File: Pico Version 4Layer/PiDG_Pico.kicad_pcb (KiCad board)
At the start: 4 copper layers, 126 x 126 mm, 71 parts, among them J1 Conn_02x05_Odd_Even, J10 Trig, J11 Laser Enable, J12 Pixel Reset, J14 Pico Socket A, J15 Pico Socket B, J16 Laser En/PWM Trig/GND, J17 USB-C PD in, J2 Conn_02x05_Odd_Even, J3 Conn_02x05_Odd_Even, J4 Conn_02x05_Odd_Even, J5 Conn_02x05_Odd_Even, J6 Conn_02x05_Odd_Even, J7 Laser 1, J8 Laser 2, U1 74LVC1G04, U10 74AHCT1G08, U12 74LVC1G17, U13 UCC27524, U14 CH224K, U15 AP63205WU, U16 LM66100, U17 LP2951D, U2 SN74LVC04AD, U3 74LVC1G04, U4 SN74LVC04AD, U5 74LVC1G04, U6 SN74LVC04AD, U7 74AHCT1G08, U8 74AHCT1G08, U9 NCP718xSN180

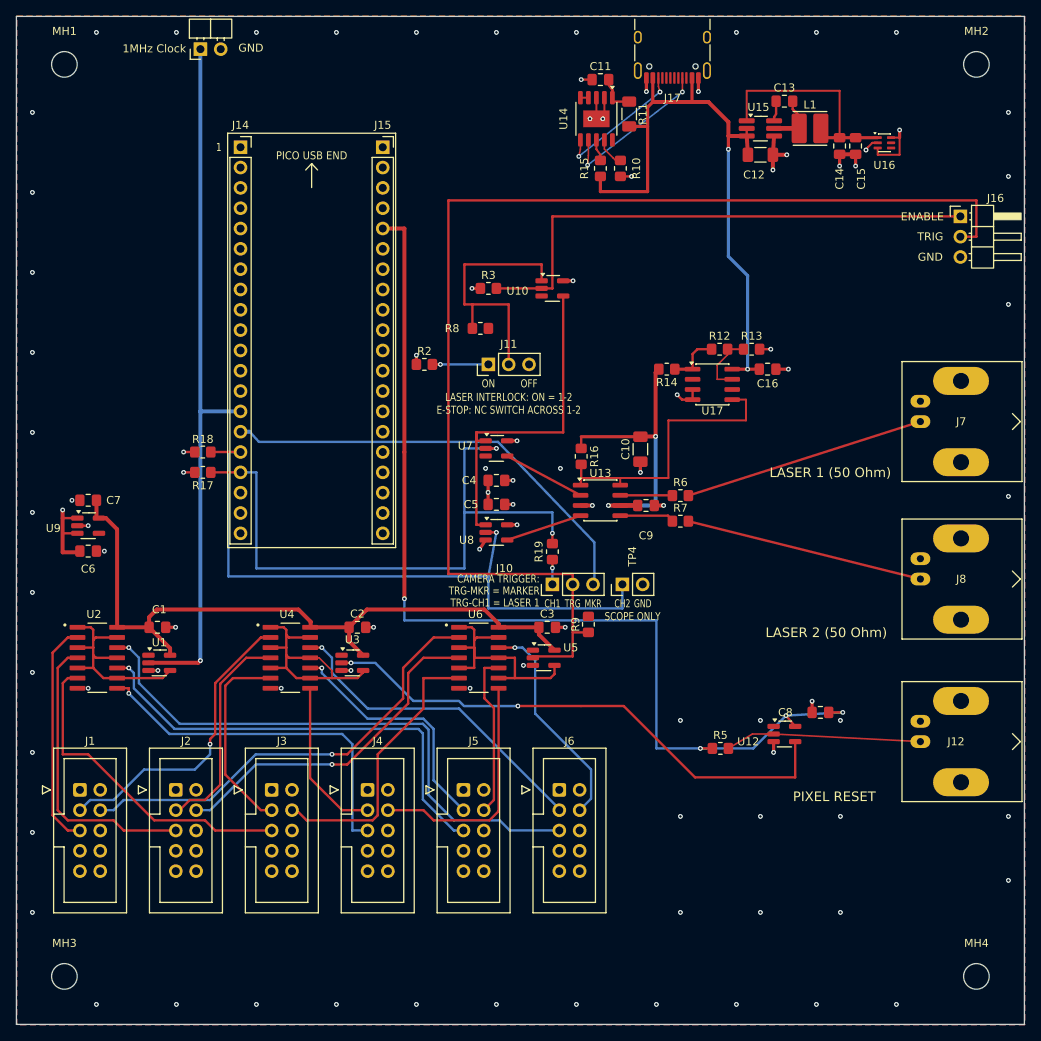
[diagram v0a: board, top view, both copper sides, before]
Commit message: Move the Pico to the top edge; label the control and power USB ports
J14/J15 and R17/R18 shifted 13.97 mm up so the Pico's micro-USB reaches the
top board edge for an enclosure cut-out. GP10-13 and 3V3 traces stretched;
PWM_Trig re-entered right of the CH1 run (crosses J15 between two unused
pads as before). CH1/CH2 lengthen equally. TP3 moved 3 mm left for socket
clearance with its spur re-jogged. Silkscreen: CONTROL / PROGRAM - PICO
MICRO-USB and POWER ONLY - USB-C PD 15 V at the two ports. DRC 0/0, all 334
pads match the schematic; gerbers, drills, zip and both placement files
regenerated; README, Hardware.md and JLC checklist updated.

Co-Authored-By: Claude Opus 5.5 (1M context) <noreply@anthropic.com>
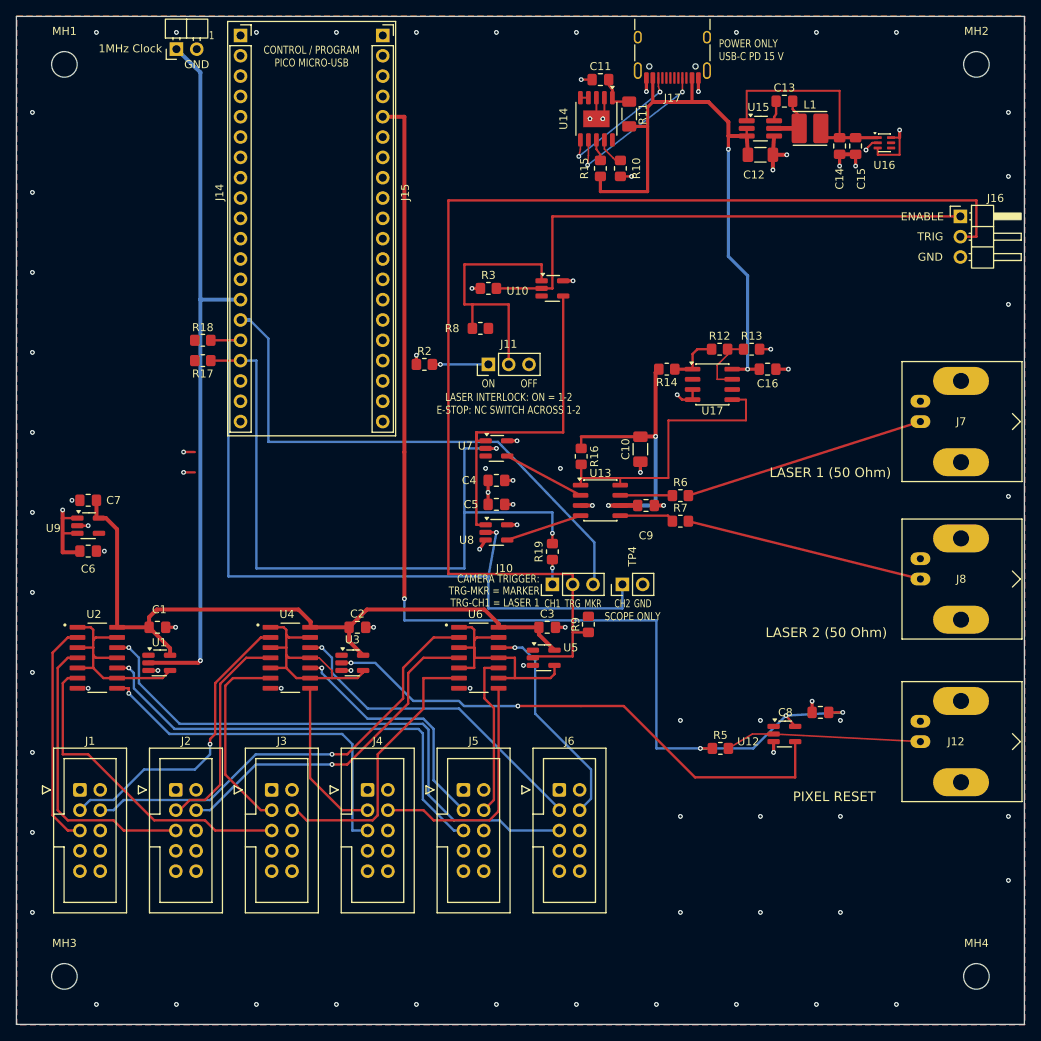
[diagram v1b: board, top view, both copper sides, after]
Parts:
- moved J14 14.0 mm to (160.0, 32.4)
- moved J15 14.0 mm to (177.8, 32.4)
- moved R17 14.0 mm to (155.3, 73.0)
- moved R18 14.0 mm to (155.3, 70.5)
- moved TP3 3.00 mm to (152.0, 34.1)
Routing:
- net _PULSE_OUT_CH2: track 84.0 -> 97.9 mm
- net _PULSE_OUT_CH1: track 79.0 -> 92.9 mm
- net +3V3: track 129.2 -> 143.2 mm
- net PWM_Trig: track 55.5 -> 68.8 mm
- net PWM_1MHz: track 88.1 -> 89.3 mm
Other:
- board text added: "CONTROL / PROGRAM"
- board text added: "PICO MICRO-USB"
- board text added: "POWER ONLY"
- board text added: "USB-C PD 15 V"
- board text removed: "PICO USB END"
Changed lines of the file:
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@@
 	(footprint "Connector_PinSocket_2.54mm:PinSocket_1x20_P2.54mm_Vertical"
 		(layer "F.Cu")
-		(at 177.795 46.355)
+		(at 177.795 32.385)
 		(descr "Through hole straight socket strip, 1x20, 2.54mm pitch, single row (from Kicad 4.0.7), script generated")
 		(tags "Through hole socket strip THT 1x20 2.54mm single row")
 		(property "Reference" "J15"
-			(at 0 -2.77 0)
+			(at 2.805 19.615 90)
 			(layer "F.SilkS")
 			(effects
@@
 	(footprint "Resistor_SMD:R_0805_2012Metric_Pad1.20x1.40mm_HandSolder"
 		(layer "F.Cu")
-		(at 155.3 86.995 180)
+		(at 155.3 73.025 180)
 		(descr "Resistor SMD 0805 (2012 Metric), square (rectangular) end terminal, IPC-7351 nominal with elongated pad for handsoldering. (Body size source: IPC-SM-782 page 72, https://www.pcb-3d.com/wordpress/wp-content/uploads/ipc-sm-782a_amendment_1_and_2.pdf)")
 		(tags "resistor handsolder")
@@
 	(footprint "Connector_PinSocket_2.54mm:PinSocket_1x20_P2.54mm_Vertical"
 		(layer "F.Cu")
-		(at 160.015 46.355)
+		(at 160.015 32.385)
 		(descr "Through hole straight socket strip, 1x20, 2.54mm pitch, single row (from Kicad 4.0.7), script generated")
 		(tags "Through hole socket strip THT 1x20 2.54mm single row")
 		(property "Reference" "J14"
-			(at 0 -2.77 0)
+			(at -2.615 19.615 90)
 			(layer "F.SilkS")
 			(effects
@@
 	(footprint "PiDG_Local:PinHeader_1x02_P2.54mm_Horizontal_EdgeTrim"
 		(layer "F.Cu")
-		(at 155.002076 34.093171 90)
+		(at 152.002076 34.093171 90)
 		(descr "Through hole angled pin header, 1x02, 2.54mm pitch, 6mm pin length, single row")
 		(tags "Through hole angled pin header THT 1x02 2.54mm single row")
@@
 	(footprint "Resistor_SMD:R_0805_2012Metric_Pad1.20x1.40mm_HandSolder"
 		(layer "F.Cu")
-		(at 155.3 84.455 180)
+		(at 155.3 70.485 180)
 		(descr "Resistor SMD 0805 (2012 Metric), square (rectangular) end terminal, IPC-7351 nominal with elongated pad for handsoldering. (Body size source: IPC-SM-782 page 72, https://www.pcb-3d.com/wordpress/wp-content/uploads/ipc-sm-782a_amendment_1_and_2.pdf)")
 		(tags "resistor handsolder")
@@
 	)
 	(gr_line
-		(start 158.405 44.6)
-		(end 179.405 44.6)
+		(start 158.405 30.63)
+		(end 179.405 30.63)
 		(stroke
 			(width 0.15)
@@
 	)
 	(gr_line
-		(start 158.405 96.4)
-		(end 158.405 44.6)
+		(start 158.405 82.43)
+		(end 158.405 30.63)
 		(stroke
 			(width 0.15)
@@
 	)
 	(gr_line
-		(start 168.905 48.4)
-		(end 168.155 49.2)
+		(start 179.405 30.63)
+		(end 179.405 82.43)
 		(stroke
 			(width 0.15)
@@
 	)
 	(gr_line
-		(start 168.905 48.4)
-		(end 168.905 51.4)
-		(stroke
-			(width 0.15)
-			(type default)
-		)
-		(layer "F.SilkS")
-	)
-	(gr_line
-		(start 168.905 48.4)
-		(end 169.655 49.2)
-		(stroke
-			(width 0.15)
-			(type default)
-		)
-		(layer "F.SilkS")
-	)
-	(gr_line
-		(start 179.405 44.6)
-		(end 179.405 96.4)
-		(stroke
-			(width 0.15)
-			(type default)
-		)
-		(layer "F.SilkS")
-	)
-	(gr_line
-		(start 179.405 96.4)
-		(end 158.405 96.4)
+		(start 179.405 82.43)
+		(end 158.405 82.43)
 		(stroke
 			(width 0.15)
@@
 		)
 	)
+	(gr_text "POWER ONLY"
+		(at 219.8 33.4 0)
+		(layer "F.SilkS")
+		(effects
+			(font
+				(size 1 0.8)
+				(thickness 0.15)
+			)
+			(justify left)
+		)
+	)
+	(gr_text "USB-C PD 15 V"
+		(at 219.8 35 0)
+		(layer "F.SilkS")
+		(effects
+			(font
+				(size 1 0.8)
+				(thickness 0.15)
+			)
+			(justify left)
+		)
+	)
 	(gr_text "1"
-		(at 157.3 46.355 0)
+		(at 156.4 32.384999 0)
+		(layer "F.SilkS")
+		(effects
+			(font
+				(size 1 0.8)
+				(thickness 0.15)
+			)
+		)
+	)
+	(gr_text "CONTROL / PROGRAM"
+		(at 168.905 34.2 0)
+		(layer "F.SilkS")
+		(effects
+			(font
+				(size 1 0.8)
+				(thickness 0.15)
+			)
+		)
+	)
+	(gr_text "PICO MICRO-USB"
+		(at 168.905 35.8 0)
 		(layer "F.SilkS")
 		(effects
@@
 		)
 	)
-	(gr_text "PICO USB END"
-		(at 168.905 47.4 0)
-		(layer "F.SilkS")
-		(effects
-			(font
-				(size 1 0.9)
-				(thickness 0.15)
-			)
-		)
-	)
-	(gr_text "GND"
-		(at 159.74 34.53 0)
+	(gr_text "1MHz Clock"
+		(at 146.24 34.03 0)
 		(layer "F.SilkS")
 		(effects
@@
 				(thickness 0.15)
 			)
-			(justify left bottom)
 		)
 	)
-	(gr_text "1MHz Clock"
-		(at 149.24 34.03 0)
+	(gr_text "ENABLE"
+		(at 245.24 55.03 0)
 		(layer "F.SilkS")
 		(effects
@@
 		)
 	)
-	(gr_text "ENABLE"
-		(at 245.24 55.03 0)
+	(gr_text "TRIG"
+		(at 246.24 57.53 0)
 		(layer "F.SilkS")
 		(effects
@@
 		)
 	)
-	(gr_text "TRIG"
-		(at 246.24 57.53 0)
+	(gr_text "GND"
+		(at 246.24 60.08 0)
 		(layer "F.SilkS")
 		(effects
@@
 	)
 	(gr_text "GND"
-		(at 246.24 60.08 0)
+		(at 154.54 36.6 0)
 		(layer "F.SilkS")
 		(effects
@@
 				(thickness 0.15)
 			)
+			(justify bottom)
 		)
 	)
@@
 	)
 	(segment
-		(start 177.795 56.515)
-		(end 180.5 56.515)
+		(start 177.795 42.545)
+		(end 180.5 42.545)
 		(width 0.5)
 		(layer "F.Cu")
@@
 	)
 	(segment
-		(start 180.5 56.515)
+		(start 180.5 42.545)
 		(end 180.5 84.455)
 		(width 0.5)
@@
 	)
 	(segment
-		(start 160.015 86.995)
-		(end 156.3 86.995)
+		(start 160.015 73.025)
+		(end 156.3 73.025)
 		(width 0.3)
 		(layer "F.Cu")
@@
 	(segment
 		(start 162 99)
-		(end 162 86.995)
+		(end 162 73.025)
 		(width 0.3)
 		(layer "B.Cu")
@@
 	)
 	(segment
-		(start 162 86.995)
-		(end 160.015 86.995)
+		(start 162 73.025)
+		(end 160.015 73.025)
 		(width 0.3)
 		(layer "B.Cu")
@@
 	)
 	(segment
-		(start 160.015 84.455)
-		(end 156.3 84.455)
+		(start 160.015 70.485)
+		(end 156.3 70.485)
 		(width 0.3)
 		(layer "F.Cu")
@@
 	(segment
 		(start 158.5 100)
-		(end 158.5 84.455)
+		(end 158.5 70.485)
 		(width 0.3)
 		(layer "B.Cu")
@@
 	)
 	(segment
-		(start 158.5 84.455)
-		(end 160.015 84.455)
+		(start 158.5 70.485)
+		(end 160.015 70.485)
 		(width 0.3)
 		(layer "B.Cu")
@@
 	)
 	(segment
-		(start 161.167 81.915)
-		(end 162.318 83.185)
+		(start 163.5 70.278)
+		(end 163.5 83.185)
+		(width 0.3)
+		(layer "B.Cu")
+		(net "PWM_Trig")
+	)
+	(segment
+		(start 161.167 67.945)
+		(end 163.5 70.278)
 		(width 0.3)
 		(layer "B.Cu")
@@
 	)
 	(segment
-		(start 160.015 81.915)
-		(end 161.167 81.915)
+		(start 160.015 67.945)
+		(end 161.167 67.945)
 		(width 0.5)
 		(layer "B.Cu")
@@
 	)
 	(segment
-		(start 162.318 83.185)
+		(start 163.5 83.185)
 		(end 192.2 83.185)
 		(width 0.3)
@@
 	)
 	(segment
-		(start 155 79.375)
-		(end 155 34.095247)
+		(start 155 65.405)
+		(end 155 37)
 		(width 0.5)
 		(layer "B.Cu")
@@
 	)
 	(segment
-		(start 160.015 79.375)
-		(end 155 79.375)
+		(start 160.015 65.405)
+		(end 155 65.405)
 		(width 0.5)
 		(layer "B.Cu")
@@
 	)
 	(segment
-		(start 155 79.375)
+		(start 155 65.405)
 		(end 155 110.53)
 		(width 0.5)
@@
 	)
 	(segment
-		(start 155 34.095247)
-		(end 155.002076 34.093171)
+		(start 155 37)
+		(end 152.002 34.093)
 		(width 0.5)
 		(layer "B.Cu")

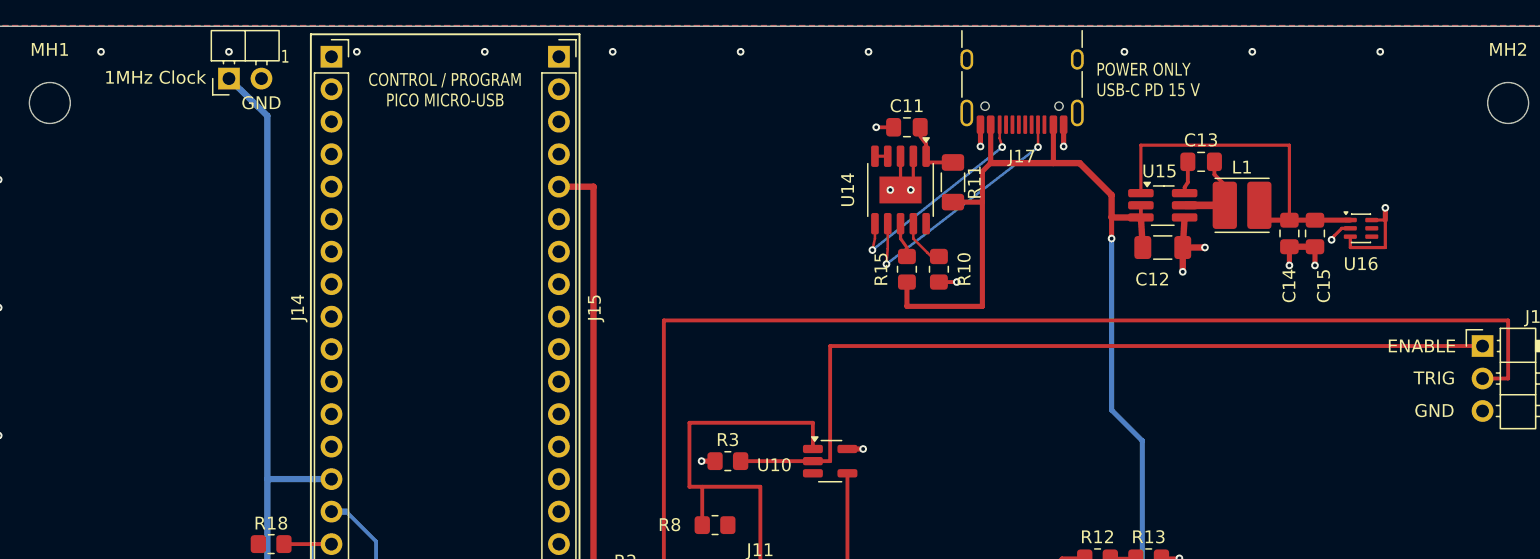
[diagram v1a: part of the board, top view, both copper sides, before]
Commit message: J16 explicit silkscreen; TP3 overhang matched to J16
J16 now reads ENABLE IN: PULL LOW = LASERS OFF / TRIG OUT: CAMERA TRIGGER
(MONITOR) / GND, plus J16: NEVER FIT A SHUNT and NOT FAIL-SAFE - PUT THE
E-STOP ON J11. TP3 moved 3.9 mm inboard so its pins overhang the top edge
by 2.1 mm, the same as J16 on the right edge (spur re-jogged, labels moved).
DRC 0/0; gerbers, drills, zip and placement files regenerated; README,
Hardware.md and JLC checklist updated.

Co-Authored-By: Claude Opus 5.5 (1M context) <noreply@anthropic.com>
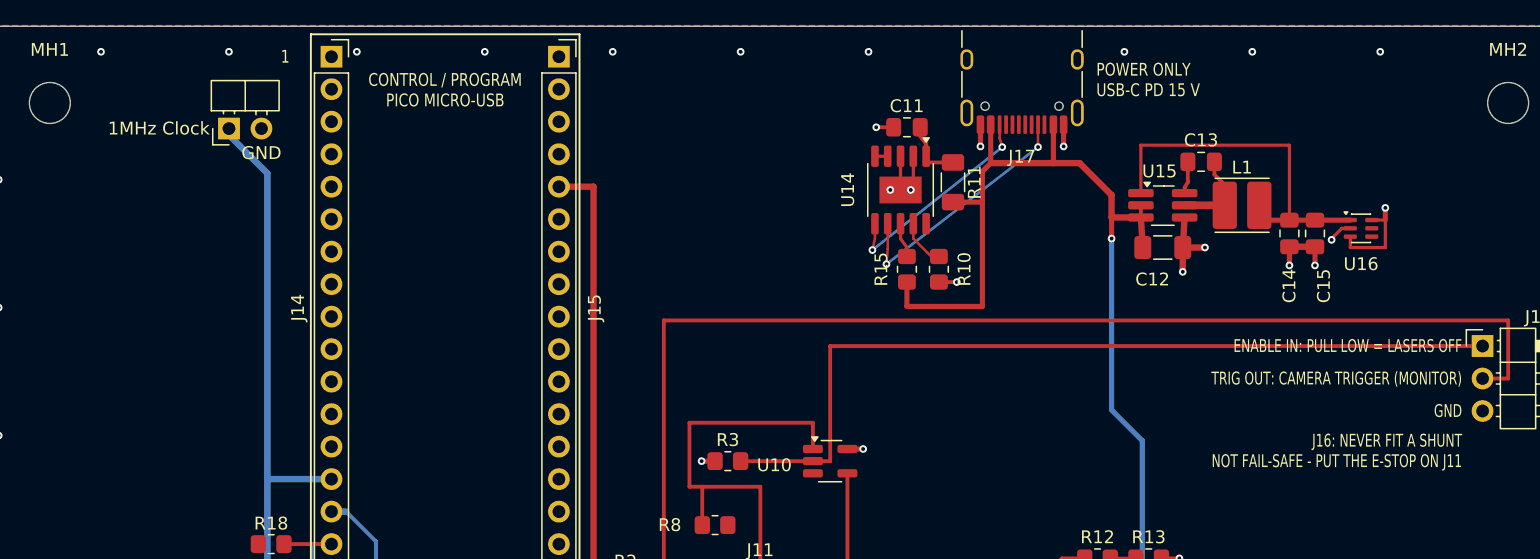
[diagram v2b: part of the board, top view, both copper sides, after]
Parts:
- moved TP3 3.91 mm to (152.0, 38.0)
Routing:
- net PWM_1MHz: track 89.3 -> 84.9 mm
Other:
- board text added: "ENABLE IN: PULL LOW = LASERS OFF"
- board text added: "J16: NEVER FIT A SHUNT"
- board text added: "NOT FAIL-SAFE - PUT THE E-STOP ON J11"
- board text added: "TRIG OUT: CAMERA TRIGGER (MONITOR)"
- board text removed: "ENABLE"
- board text removed: "TRIG"
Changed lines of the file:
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@@
 	(footprint "PiDG_Local:PinHeader_1x02_P2.54mm_Horizontal_EdgeTrim"
 		(layer "F.Cu")
-		(at 152.002076 34.093171 90)
+		(at 152.002076 38 90)
 		(descr "Through hole angled pin header, 1x02, 2.54mm pitch, 6mm pin length, single row")
 		(tags "Through hole angled pin header THT 1x02 2.54mm single row")
@@
 		)
 	)
+	(gr_text "ENABLE IN: PULL LOW = LASERS OFF"
+		(at 248.4 55 0)
+		(layer "F.SilkS")
+		(effects
+			(font
+				(size 1 0.7)
+				(thickness 0.15)
+			)
+			(justify right)
+		)
+	)
+	(gr_text "TRIG OUT: CAMERA TRIGGER (MONITOR)"
+		(at 248.4 57.54 0)
+		(layer "F.SilkS")
+		(effects
+			(font
+				(size 1 0.7)
+				(thickness 0.15)
+			)
+			(justify right)
+		)
+	)
+	(gr_text "GND"
+		(at 248.4 60.08 0)
+		(layer "F.SilkS")
+		(effects
+			(font
+				(size 1 0.7)
+				(thickness 0.15)
+			)
+			(justify right)
+		)
+	)
+	(gr_text "J16: NEVER FIT A SHUNT"
+		(at 248.4 62.4 0)
+		(layer "F.SilkS")
+		(effects
+			(font
+				(size 1 0.7)
+				(thickness 0.15)
+			)
+			(justify right)
+		)
+	)
+	(gr_text "NOT FAIL-SAFE - PUT THE E-STOP ON J11"
+		(at 248.4 64 0)
+		(layer "F.SilkS")
+		(effects
+			(font
+				(size 1 0.7)
+				(thickness 0.15)
+			)
+			(justify right)
+		)
+	)
 	(gr_text "POWER ONLY"
 		(at 219.8 33.4 0)
@@
 		)
 	)
-	(gr_text "1MHz Clock"
-		(at 146.24 34.03 0)
-		(layer "F.SilkS")
-		(effects
-			(font
-				(size 1 1)
-				(thickness 0.15)
-			)
-		)
-	)
-	(gr_text "ENABLE"
-		(at 245.24 55.03 0)
-		(layer "F.SilkS")
-		(effects
-			(font
-				(size 1 1)
-				(thickness 0.15)
-			)
-		)
-	)
-	(gr_text "TRIG"
-		(at 246.24 57.53 0)
-		(layer "F.SilkS")
-		(effects
-			(font
-				(size 1 1)
-				(thickness 0.15)
-			)
-		)
-	)
 	(gr_text "GND"
-		(at 246.24 60.08 0)
+		(at 154.542075 40.5 0)
 		(layer "F.SilkS")
 		(effects
@@
 				(thickness 0.15)
 			)
+			(justify bottom)
 		)
 	)
-	(gr_text "GND"
-		(at 154.54 36.6 0)
+	(gr_text "1MHz Clock"
+		(at 150.502076 38 0)
 		(layer "F.SilkS")
 		(effects
@@
 				(thickness 0.15)
 			)
-			(justify bottom)
+			(justify right)
 		)
 	)
@@
 	(segment
 		(start 155 65.405)
-		(end 155 37)
+		(end 155 41.5)
 		(width 0.5)
 		(layer "B.Cu")
@@
 	)
 	(segment
-		(start 155 37)
-		(end 152.002 34.093)
+		(start 155 41.5)
+		(end 152.002076 38.5)
 		(width 0.5)
 		(layer "B.Cu")
